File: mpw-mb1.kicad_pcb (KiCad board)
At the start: 2 copper layers, 104.5 x 81 mm, 285 parts, among them J1 Conn_01x06, J10 61302411121, J11 61302411121, J12 Conn_01x02, J2 Conn_02x02_Odd_Even, J3 613012243121, J4 Conn_01x02, J5 Conn_01x03, J6 UJC-HP-3-SMT-TR, J7 TT03_BREAKOUT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

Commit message: logo, logo, everywhere but not a drop to drink
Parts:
- added G***: LOGO, LOGO, B.Cu at (134.1, 80.2)
- added G***: LOGO, LOGO, B.Cu at (134.0, 84.4)
- added REF**: OSHW_BADGE, OSHW:OSHW_BADGE, F.Cu at (107.3, 113.2)
- added REF**: Z2A_logo, Logos:Z2A_logo, B.Cu at (134.0, 95.5)
- added REF**: OSHW_BADGE, OSHW:OSHW_BADGE, B.Cu at (134.0, 114.5)
- added REF**: TT_logo, Logos:TT_logo, B.Cu at (134.0, 64.9)
- moved REF** 13.5 mm to (107.3, 94.1)
- moved G*** 6.07 mm to (107.3, 83.1)
- moved G*** 5.54 mm to (107.2, 78.9)

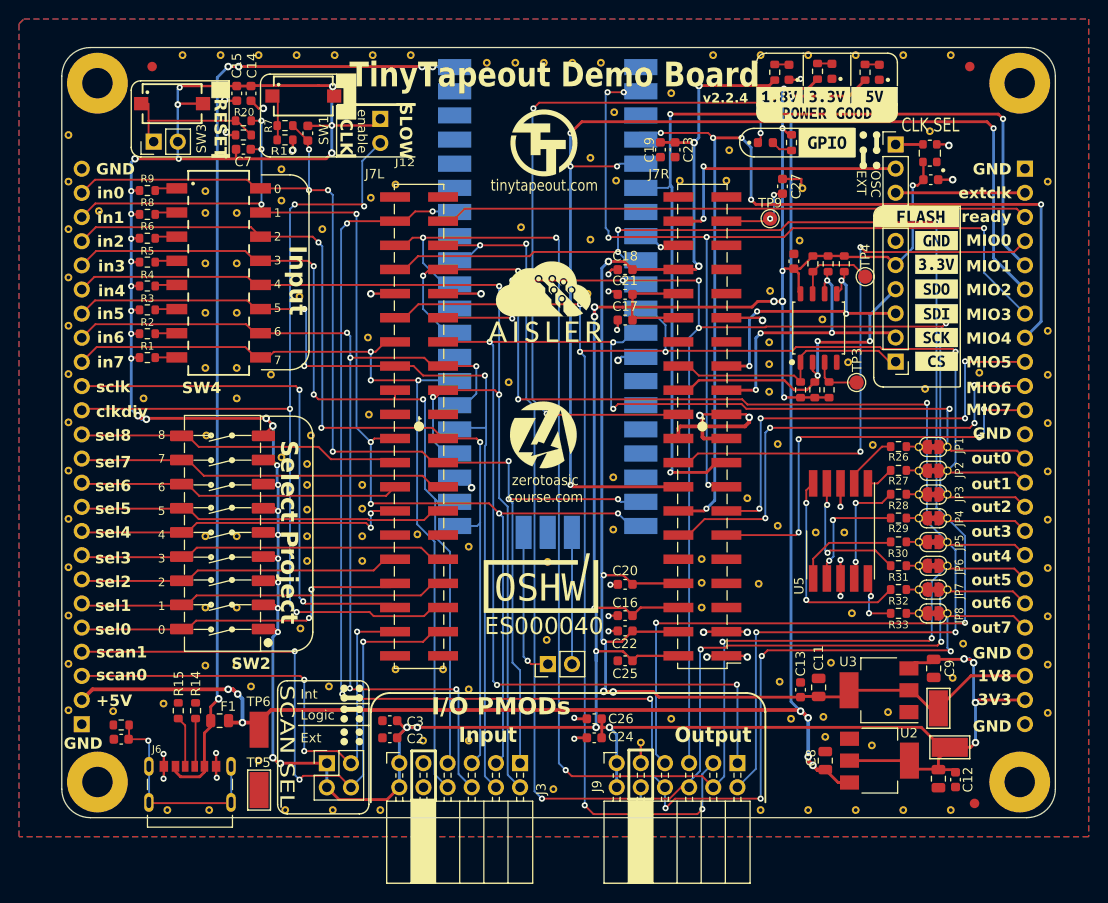
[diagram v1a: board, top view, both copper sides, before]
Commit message: v2.2.5: 7-seg fp, new osc, nRST pull-up
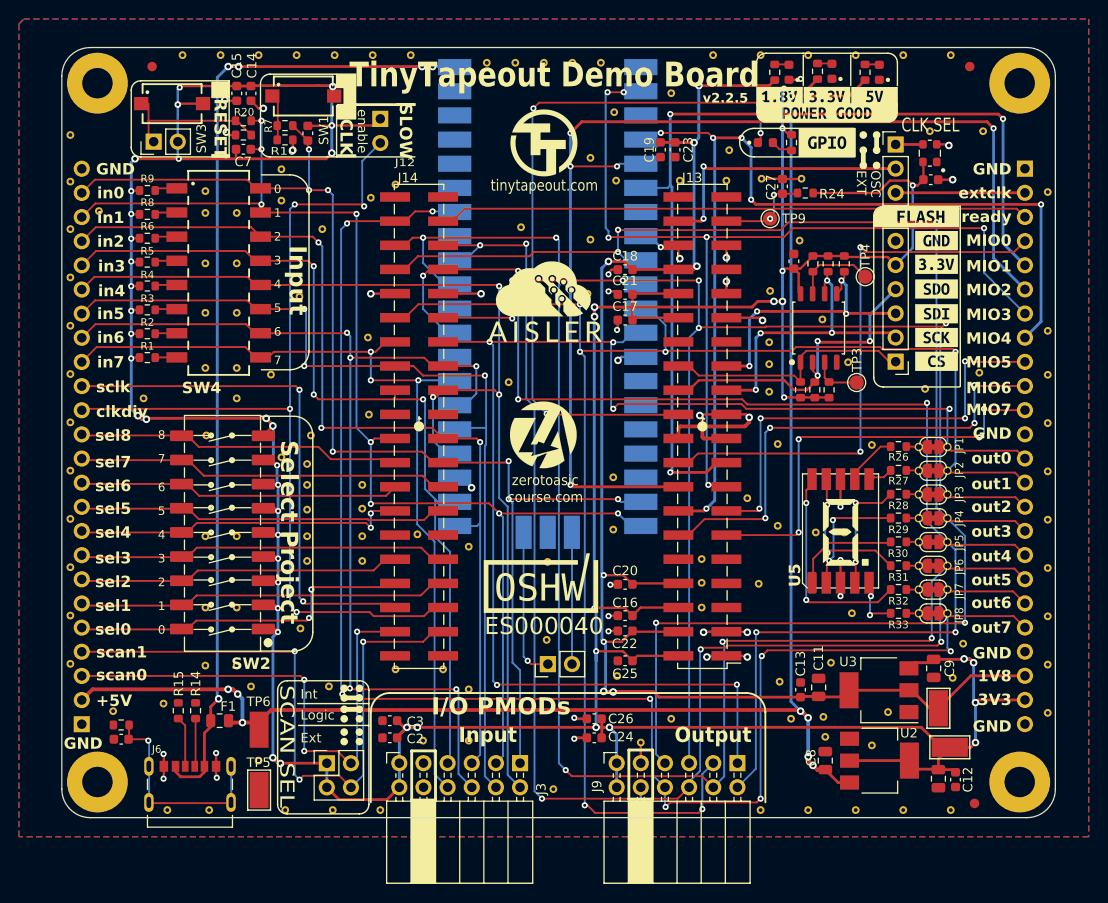
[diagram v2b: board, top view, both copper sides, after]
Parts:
- removed the STITCH13 at (117.4, 133.3)
- removed STITCH34: StitchingVia-0.4mmDrill, flyingcarsfootprints:StitchingVia-0.4mmDrill
- added R24: 10k, Resistor_SMD:R_0603_1608Metric, F.Cu at (134.7, 68.8)
- added STITCH: StitchingVia-0.4mmDrill, flyingcarsfootprints:StitchingVia-0.4mmDrill, F.Cu at (130.1, 67.3)
- added STITCH: StitchingVia-0.4mmDrill, flyingcarsfootprints:StitchingVia-0.4mmDrill, F.Cu at (153.4, 62.3)
- added STITCH23: StitchingVia-0.4mmDrill, flyingcarsfootprints:StitchingVia-0.4mmDrill, F.Cu at (114.9, 119.6)
- U5: footprint Display_7Segment:KCSC02-106 -> TinyTapeout:WL_S7DS-157112V12700
- X1: value 10MHz -> 20MHz
- moved STITCH 1.10 mm to (160.2, 68.7)
- moved STITCH 1.00 mm to (134.3, 67.3)
- moved STITCH 0.20 mm to (57.4, 67.6)
- moved STITCH 0.20 mm to (57.4, 62.7)
- moved STITCH20 0.20 mm to (57.4, 72.6)
- moved STITCH24 0.20 mm to (57.4, 77.7)
- moved STITCH26 0.20 mm to (57.4, 82.8)
- moved STITCH27 0.20 mm to (57.4, 87.8)
- moved STITCH28 0.20 mm to (57.4, 92.9)
- moved STITCH29 0.20 mm to (57.4, 98.0)
- moved STITCH30 0.20 mm to (57.4, 103.1)
- moved STITCH31 0.20 mm to (57.4, 108.2)
- moved STITCH32 0.20 mm to (57.4, 113.2)
- moved STITCH33 0.20 mm to (57.4, 118.3)
- moved STITCH23 0.10 mm to (141.7, 95.3)
- renumbered J7R to J13, J7L to J14
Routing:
- net +3.3V: track 472.8 -> 484.0 mm
- net GND: track 84.5 -> 89.3 mm, vias 34 -> 38
- net /~{SOC_RST}: track 8.33 -> 9.93 mm
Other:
- board text added: "v2.2.5"
- board text removed: "v2.2.4"

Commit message: PCBA BOM, viewer and gerbers
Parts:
- J12: value Conn_01x02 -> 61300211121

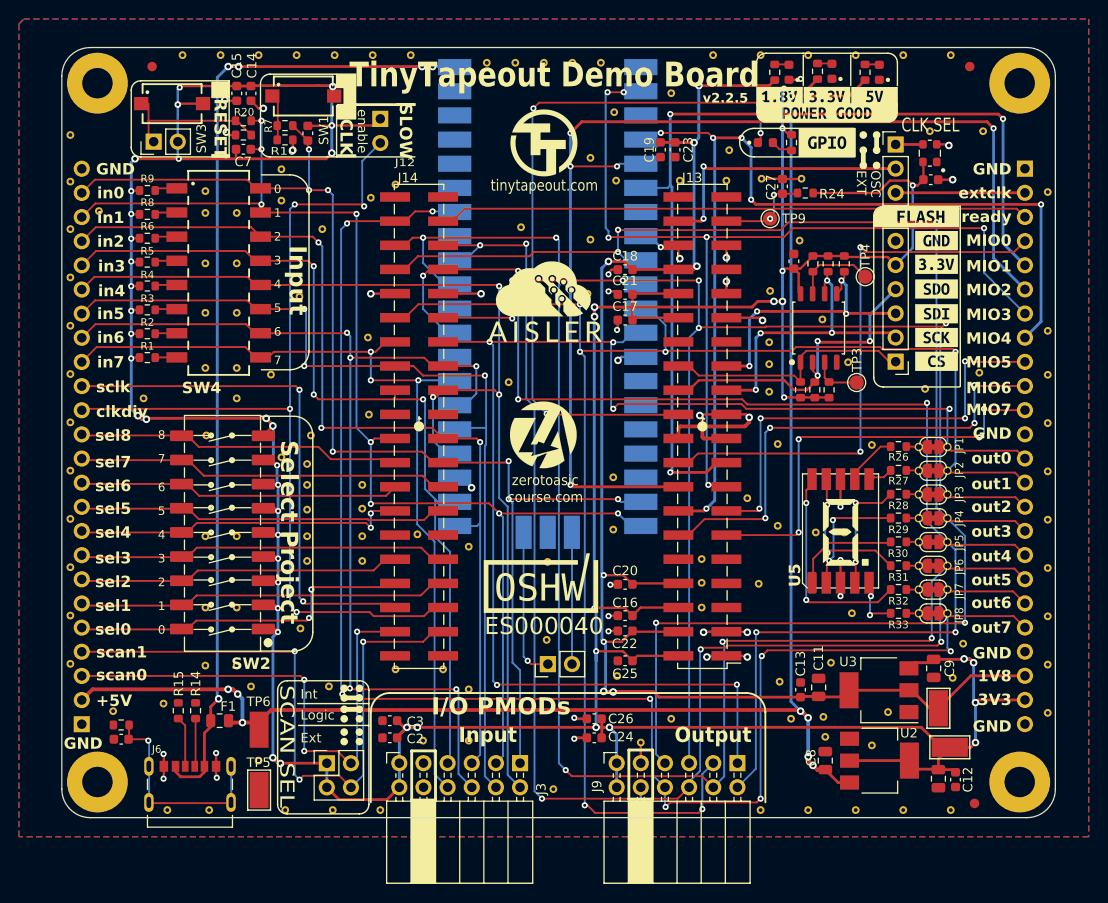
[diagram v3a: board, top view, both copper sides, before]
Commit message: v2.2.6 logo mods, BOM adjust, minor silk tweaks
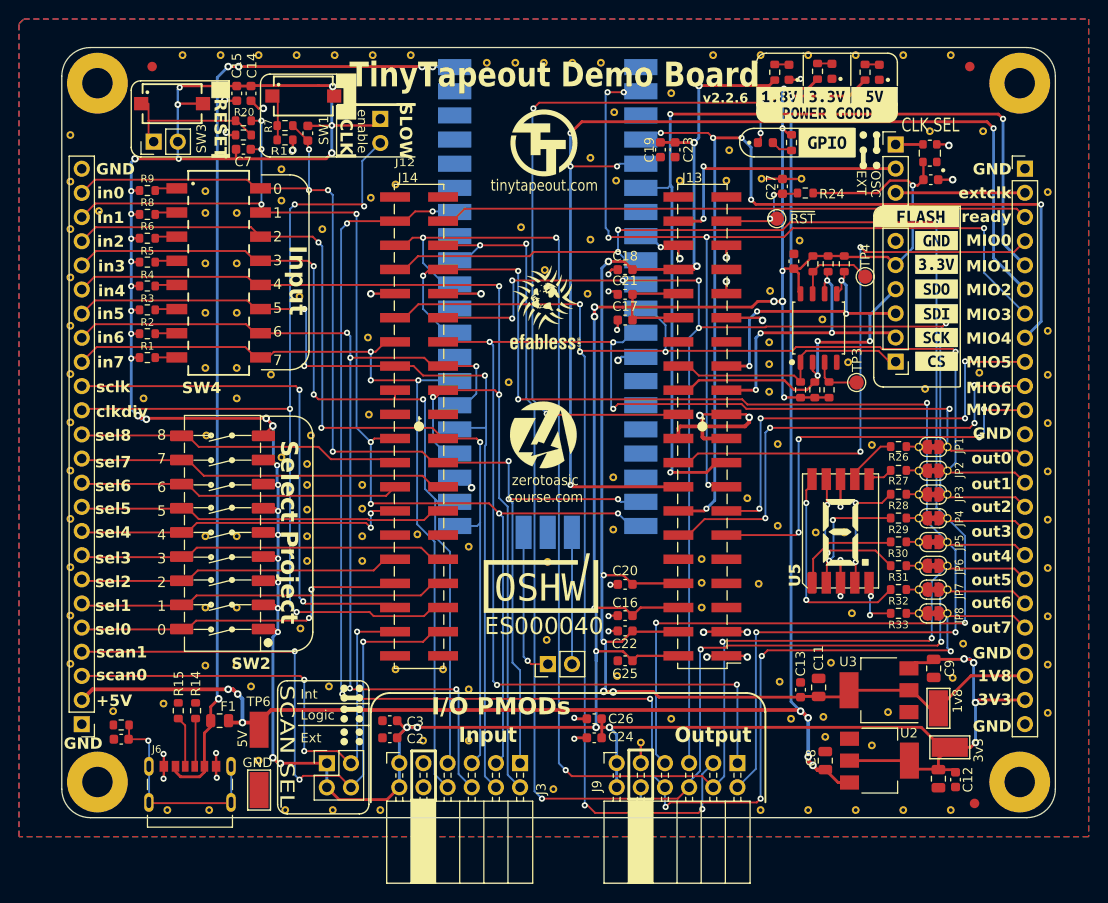
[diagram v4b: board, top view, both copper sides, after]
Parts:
- removed the G*** at (107.2, 78.9)
- removed the G*** at (107.3, 83.1)
- removed the G*** at (81.3, 80.0)
- removed the G*** at (134.1, 80.2)
- removed the G*** at (134.0, 84.4)
- added G***: LOGO, flyingcarsfootprints:PsychoLogoSmall, B.Cu at (80.5, 93.5)
- added REF**: Logo, Logos:ef_logo_graphical, F.Cu at (107.3, 79.8)
- added REF**: Logo, Logos:ef_logo, F.Cu at (107.3, 84.5)
- added REF**: Logo, Logos:ef_logo_graphical, B.Cu at (133.5, 85.4)
- added REF**: Logo, Logos:ef_logo, B.Cu at (133.5, 90.1)
- J10, J11: moved to F.Cu
- moved REF** 54.7 mm to (80.0, 105.5)
- moved REF** 6.68 mm to (133.5, 71.6)
- moved REF** 5.04 mm to (133.5, 100.5)
- moved TP9 0.70 mm to (131.7, 71.5)
- turned J10 to 180 degrees
- turned J11 to 0 degrees
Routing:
- net /~{SOC_RST}: track 9.93 -> 10.6 mm
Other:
- board text added: "(C) 2023, 2024 TinyTapeout"
- board text added: "1v8"
- board text added: "5V"
- board text added: "Designed by Pat Deegan psychogenic.com"
- board text added: "v2.2.6"
- board text added: "~{RST}"
- board text removed: "(C) 2023 Pat Deegan https://psychogenic.com"
- board text removed: "v2.2.5"

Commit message: adjustments for cleaner gnd fills
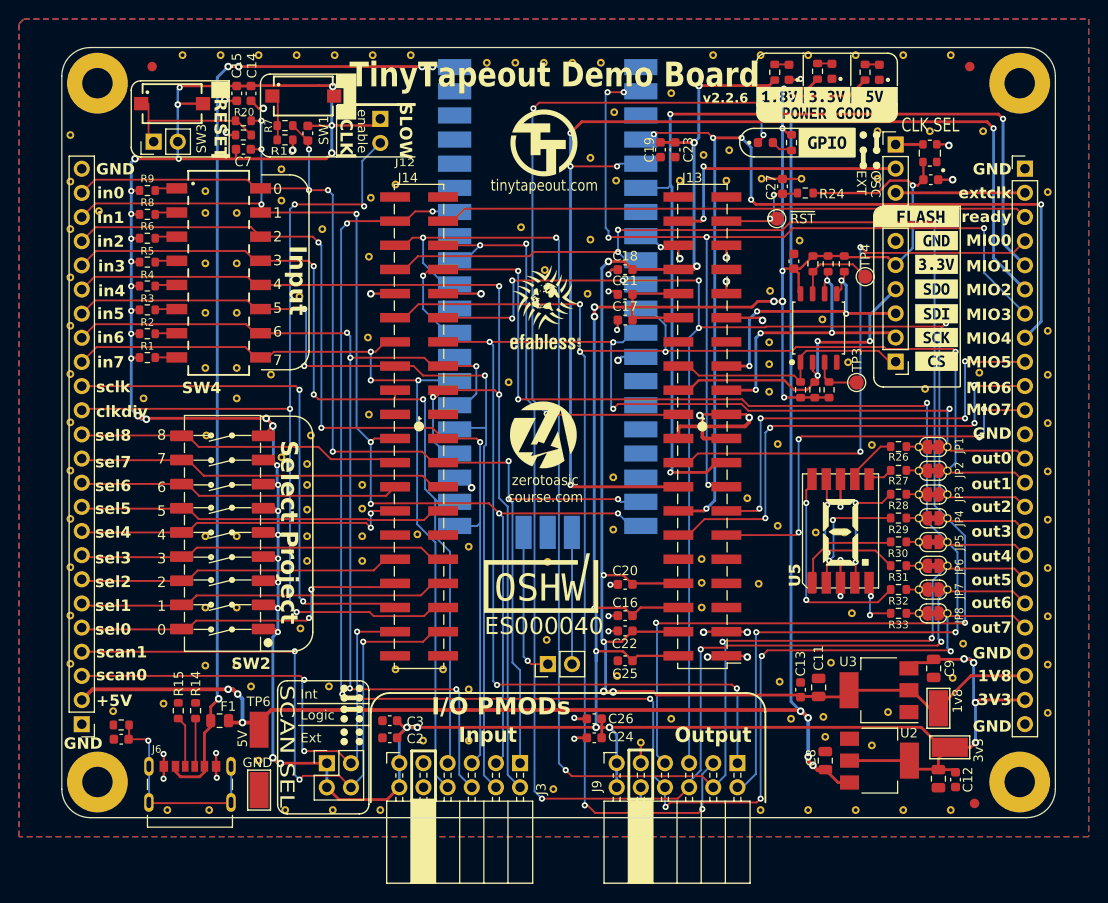
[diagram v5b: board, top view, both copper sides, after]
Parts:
- added STITCH: StitchingVia-0.4mmDrill, flyingcarsfootprints:StitchingVia-0.4mmDrill, F.Cu at (142.3, 62.3)
- added STITCH: StitchingVia-0.4mmDrill, flyingcarsfootprints:StitchingVia-0.4mmDrill, F.Cu at (142.3, 67.3)
- added STITCH: StitchingVia-0.4mmDrill, flyingcarsfootprints:StitchingVia-0.4mmDrill, F.Cu at (88.8, 75.5)
- added STITCH23: StitchingVia-0.4mmDrill, flyingcarsfootprints:StitchingVia-0.4mmDrill, F.Cu at (124.0, 64.8)
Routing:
- net out4: track 148.1 -> 148.7 mm
